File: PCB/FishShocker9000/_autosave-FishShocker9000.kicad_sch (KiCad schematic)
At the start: 205 parts, among them J1 Barrel_Jack, J10 P70-1000045R, J100 P70-1000045R, J101 P70-1000045R, J102 P70-1000045R, J103 P70-1000045R, J104 P70-1000045R, J105 P70-1000045R, J106 P70-1000045R, J107 P70-1000045R, J108 P70-1000045R, J109 P70-1000045R, J11 P70-1000045R, J110 P70-1000045R, J111 P70-1000045R, J112 P70-1000045R, J113 P70-1000045R, J114 P70-1000045R, J115 P70-1000045R, J116 P70-1000045R, J117 P70-1000045R, J118 P70-1000045R, J119 P70-1000045R, J12 P70-1000045R, J120 P70-1000045R, J121 P70-1000045R, J122 P70-1000045R, J123 P70-1000045R, J124 P70-1000045R, J125 P70-1000045R, J126 P70-1000045R, J127 P70-1000045R, J128 P70-1000045R, J129 P70-1000045R, J13 P70-1000045R, J130 P70-1000045R, J131 P70-1000045R, J132 P70-1000045R, J133 P70-1000045R, J134 P70-1000045R, J135 P70-1000045R, J136 P70-1000045R, J137 P70-1000045R, J138 P70-1000045R, J139 P70-1000045R, J14 P70-1000045R, J140 P70-1000045R, J141 P70-1000045R, J142 P70-1000045R, J143 P70-1000045R, J144 P70-1000045R, J145 P70-1000045R, J15 P70-1000045R, J16 P70-1000045R, J17 P70-1000045R, J18 P70-1000045R, J19 P70-1000045R, J2 P70-1000045R, J20 P70-1000045R, J21 P70-1000045R, J22 P70-1000045R, J23 P70-1000045R, J24 P70-1000045R, J25 P70-1000045R, J26 P70-1000045R, J27 P70-1000045R, J28 P70-1000045R, J29 P70-1000045R, J3 P70-1000045R, J30 P70-1000045R, J31 P70-1000045R, J32 P70-1000045R, J33 P70-1000045R, J34 P70-1000045R, J35 P70-1000045R, J36 P70-1000045R, J37 P70-1000045R, J38 P70-1000045R, J39 P70-1000045R, J4 P70-1000045R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

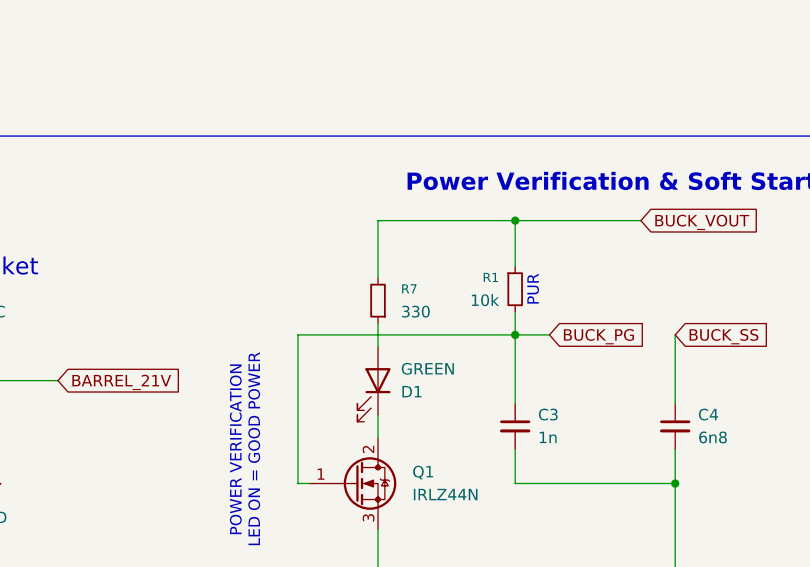
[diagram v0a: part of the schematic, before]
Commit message: Placed Pogo Pins
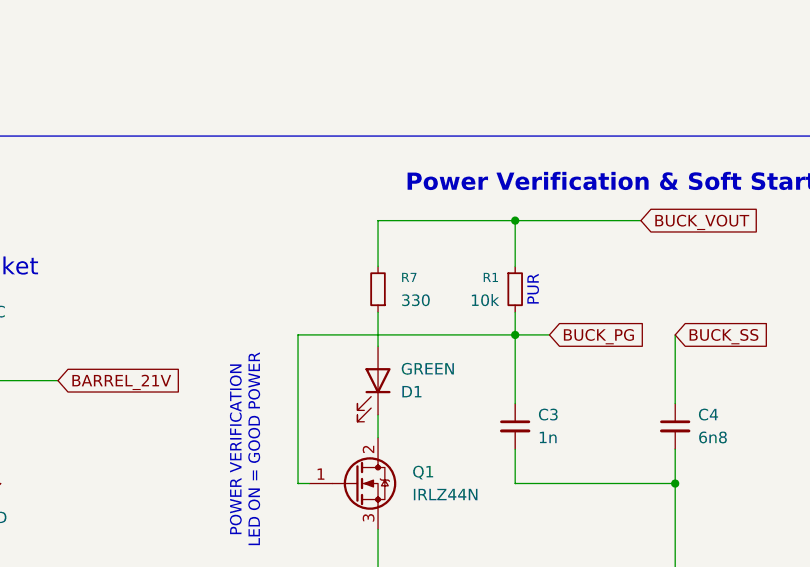
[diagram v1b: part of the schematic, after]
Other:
- moved on the sheet: R7
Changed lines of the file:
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@@
 	(wire
 		(pts
-			(xy 91.44 33.02) (xy 91.44 35.56)
+			(xy 91.44 31.75) (xy 91.44 35.56)
 		)
 		(stroke
@@
 	(wire
 		(pts
-			(xy 91.44 21.59) (xy 91.44 27.94)
+			(xy 91.44 21.59) (xy 91.44 26.67)
 		)
 		(stroke
@@
 	(symbol
 		(lib_id "Device:R_Small")
-		(at 91.44 30.48 180)
+		(at 91.44 29.21 180)
 		(unit 1)
 		(exclude_from_sim no)
@@
 		(fields_autoplaced yes)
 		(property "Reference" "R7"
-			(at 93.98 29.2099 0)
+			(at 93.98 27.9399 0)
 			(effects
 				(font
@@
 		)
 		(property "Value" "330"
-			(at 93.98 31.7499 0)
+			(at 93.98 30.4799 0)
 			(effects
 				(font
@@
 		)
 		(property "Footprint" "Resistor_SMD:R_0805_2012Metric"
-			(at 91.44 30.48 0)
+			(at 91.44 29.21 0)
 			(effects
 				(font
@@
 		)
 		(property "Datasheet" "~"
-			(at 91.44 30.48 0)
+			(at 91.44 29.21 0)
 			(effects
 				(font
@@
 		)
 		(property "Description" "Resistor, small symbol"
-			(at 91.44 30.48 0)
+			(at 91.44 29.21 0)
 			(effects
 				(font
